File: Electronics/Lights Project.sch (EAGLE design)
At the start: 16 parts

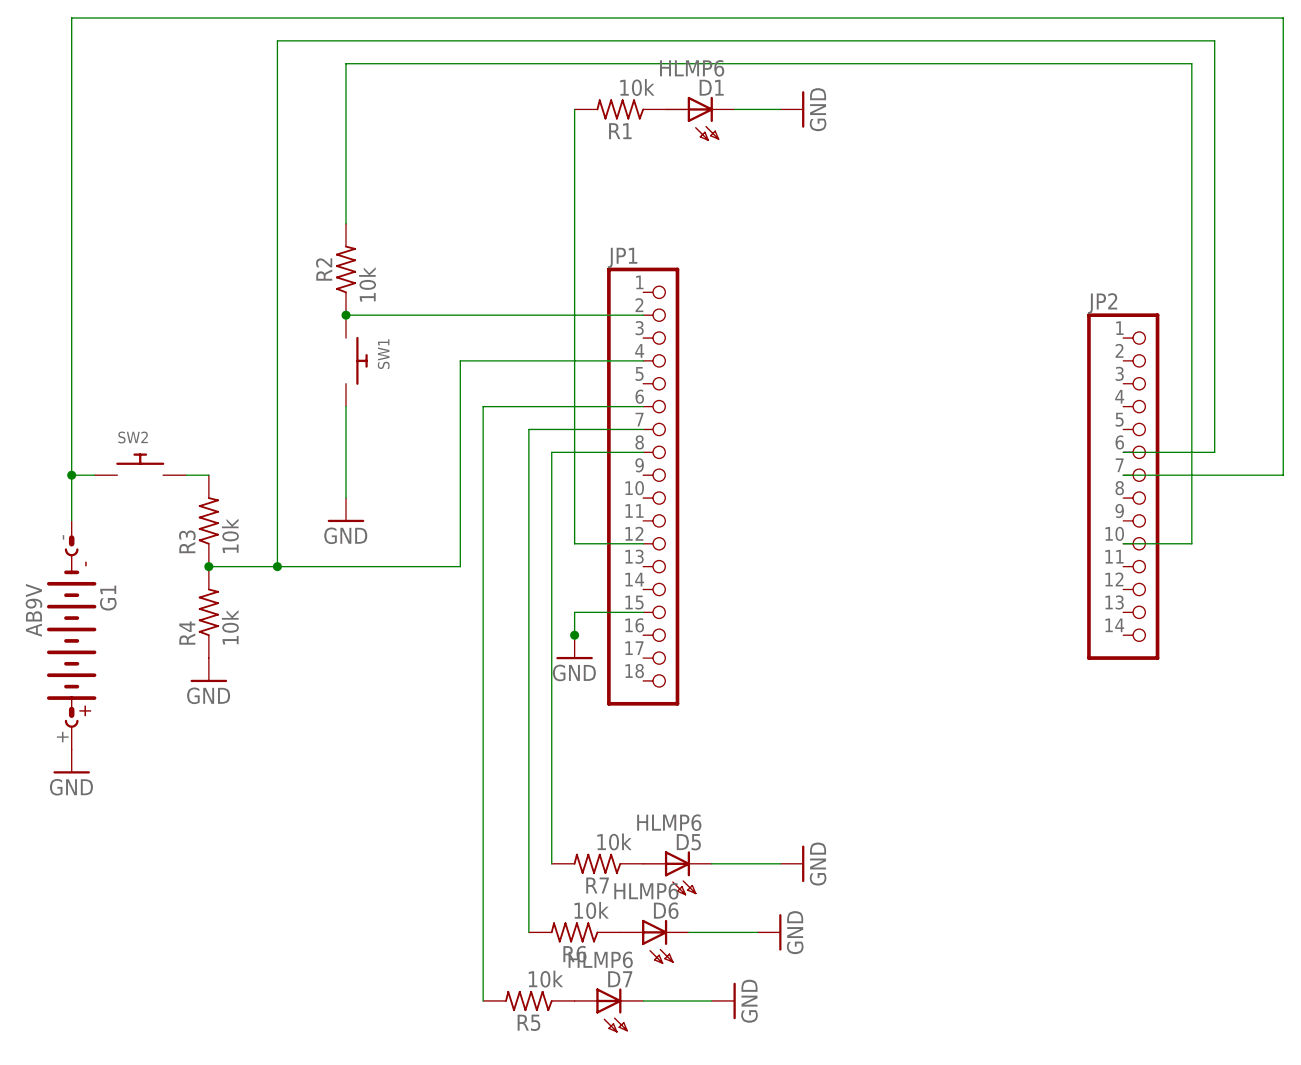
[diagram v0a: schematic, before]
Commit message: Updated PCB and Schematic: added headers and holes
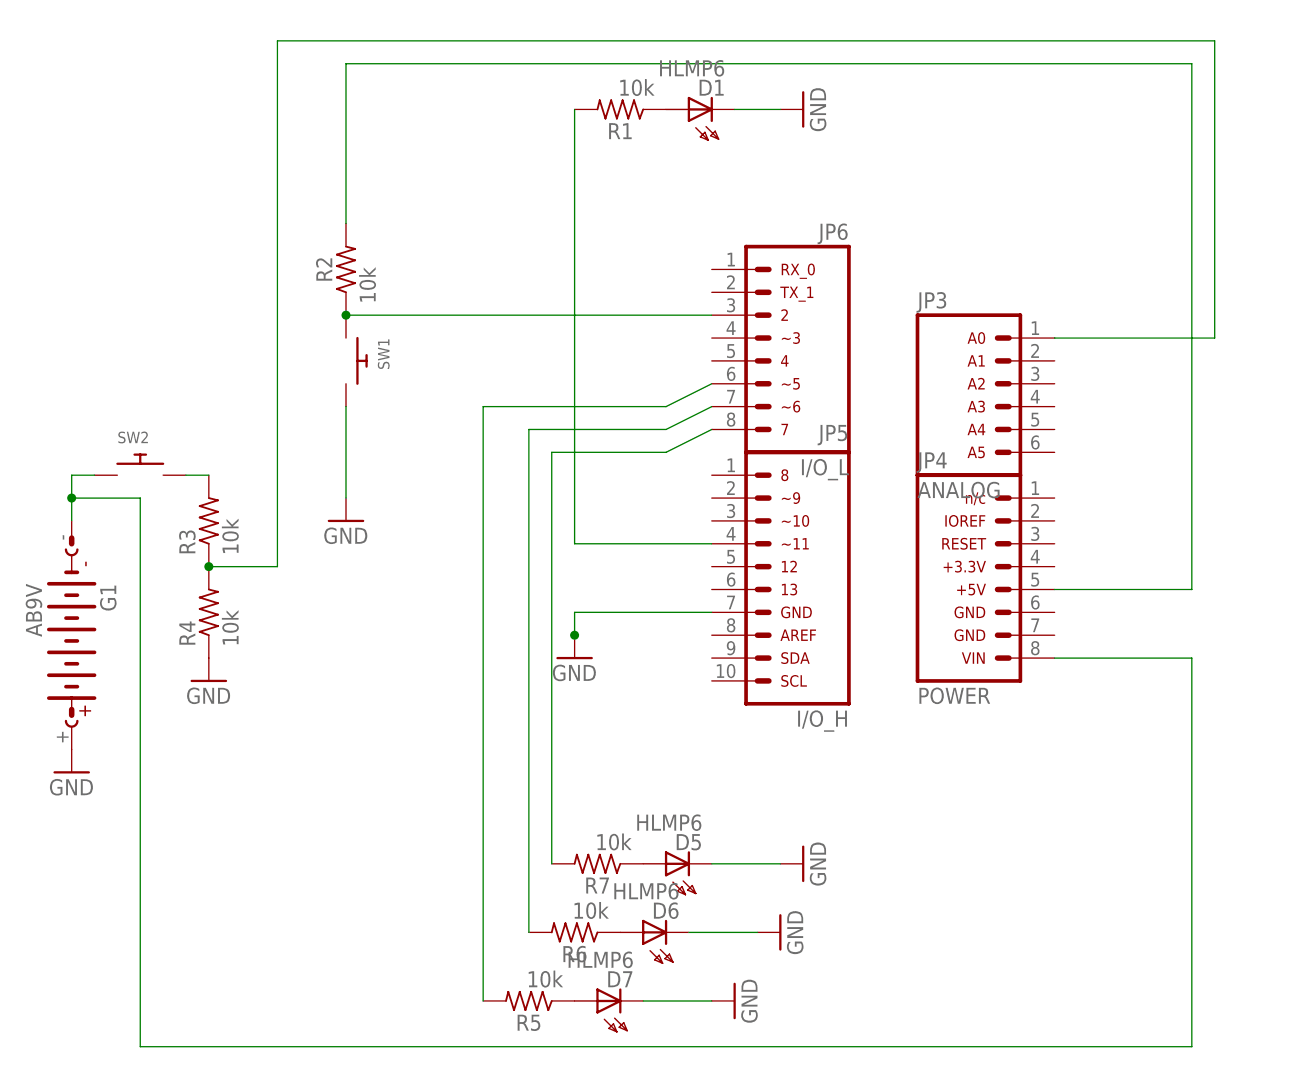
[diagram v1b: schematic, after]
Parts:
- removed JP1: (no value), adafruit:PINHD-1X18
- removed JP2: (no value), adafruit:PINHD-1X14
- added JP3: (no value), arduino_jw:ARDUINO_CONN-ANALOGSIP
- added JP4: (no value), arduino_jw:ARDUINO_CONN-POWERSIP
- added JP5: ARDUINO_CONN-IO_HSIP, arduino_jw:ARDUINO_CONN-IO_HSIP
- added JP6: (no value), arduino_jw:ARDUINO_CONN-IO_LSIP
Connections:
- net GND: now also JP5.7; no longer JP1.15
- net N$1: now also JP4.8; no longer JP2.7
- net N$10: now also JP6.7; no longer JP1.7
- net N$11: now also JP6.8; no longer JP1.8
- net N$13: now also JP3.1; no longer JP1.4, JP2.6
- net N$14: now also JP4.5; no longer JP2.10
- net N$2: now also JP5.4; no longer JP1.12
- net N$5: now also JP6.3; no longer JP1.2
- net N$8: now also JP6.6; no longer JP1.6
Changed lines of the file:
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@@
 <part name="GND10" library="supply1" library_urn="urn:adsk.eagle:library:371" deviceset="GND" device=""/>
 <part name="R7" library="rcl" library_urn="urn:adsk.eagle:library:334" deviceset="R-US_" device="R0805" package3d_urn="urn:adsk.eagle:package:23553/2" value="10k"/>
-<part name="JP1" library="adafruit" library_urn="urn:adsk.eagle:library:420" deviceset="PINHD-1X18" device="" package3d_urn="urn:adsk.eagle:package:6240826/1"/>
-<part name="JP2" library="adafruit" library_urn="urn:adsk.eagle:library:420" deviceset="PINHD-1X14" device="" package3d_urn="urn:adsk.eagle:package:6240769/1"/>
 <part name="D1" library="display-hp" library_urn="urn:adsk.eagle:library:212" deviceset="HLMP6" device="" package3d_urn="urn:adsk.eagle:package:12992/1"/>
 <part name="D5" library="display-hp" library_urn="urn:adsk.eagle:library:212" deviceset="HLMP6" device="" package3d_urn="urn:adsk.eagle:package:12992/1"/>
 <part name="D6" library="display-hp" library_urn="urn:adsk.eagle:library:212" deviceset="HLMP6" device="" package3d_urn="urn:adsk.eagle:package:12992/1"/>
 <part name="D7" library="display-hp" library_urn="urn:adsk.eagle:library:212" deviceset="HLMP6" device="" package3d_urn="urn:adsk.eagle:package:12992/1"/>
+<part name="JP3" library="arduino_jw" deviceset="ARDUINO_CONN-ANALOG" device="SIP"/>
+<part name="JP5" library="arduino_jw" deviceset="ARDUINO_CONN-IO_H" device="SIP"/>
+<part name="JP6" library="arduino_jw" deviceset="ARDUINO_CONN-IO_L" device="SIP"/>
+<part name="JP4" library="arduino_jw" deviceset="ARDUINO_CONN-POWER" device="SIP"/>
 </parts>
 <sheets>
@@
 <attribute name="NAME" x="63.5" y="-6.604" size="1.778" layer="95" font="vector" rot="R180" align="bottom-center"/>
 </instance>
-<instance part="JP1" gate="A" x="71.12" y="38.1">
-<attribute name="NAME" x="64.77" y="61.595" size="1.778" layer="95"/>
-<attribute name="VALUE" x="64.77" y="10.16" size="1.778" layer="96"/>
-</instance>
-<instance part="JP2" gate="A" x="124.46" y="38.1">
-<attribute name="NAME" x="118.11" y="56.515" size="1.778" layer="95"/>
-<attribute name="VALUE" x="118.11" y="15.24" size="1.778" layer="96"/>
-</instance>
 <instance part="D1" gate="A" x="76.2" y="78.74" rot="R90">
 <attribute name="NAME" x="77.724" y="82.042" size="1.778" layer="95" rot="R180"/>
@@
 <attribute name="NAME" x="67.564" y="-17.018" size="1.778" layer="95" rot="R180"/>
 <attribute name="VALUE" x="67.564" y="-14.859" size="1.778" layer="96" rot="R180"/>
+</instance>
+<instance part="JP3" gate="G$1" x="99.06" y="38.1">
+<attribute name="NAME" x="99.06" y="56.642" size="1.778" layer="95"/>
+</instance>
+<instance part="JP5" gate="G$1" x="91.44" y="12.7" rot="MR0">
+<attribute name="NAME" x="91.44" y="41.91" size="1.778" layer="95" rot="MR0"/>
+</instance>
+<instance part="JP6" gate="G$1" x="91.44" y="40.64" rot="MR0">
+<attribute name="NAME" x="91.44" y="64.262" size="1.778" layer="95" rot="MR0"/>
+</instance>
+<instance part="JP4" gate="G$1" x="99.06" y="15.24">
+<attribute name="NAME" x="99.06" y="38.862" size="1.778" layer="95"/>
 </instance>
 </instances>
@@
 <segment>
 <pinref part="G1" gate="G$1" pin="-"/>
-<wire x1="5.08" y1="33.02" x2="5.08" y2="38.1" width="0.1524" layer="91"/>
+<wire x1="5.08" y1="33.02" x2="5.08" y2="35.56" width="0.1524" layer="91"/>
 <pinref part="SW2" gate="G$1" pin="P$1"/>
+<wire x1="5.08" y1="35.56" x2="5.08" y2="38.1" width="0.1524" layer="91"/>
 <wire x1="5.08" y1="38.1" x2="7.62" y2="38.1" width="0.1524" layer="91"/>
-<junction x="5.08" y="38.1"/>
-<wire x1="5.08" y1="38.1" x2="5.08" y2="88.9" width="0.1524" layer="91"/>
-<wire x1="5.08" y1="88.9" x2="139.7" y2="88.9" width="0.1524" layer="91"/>
-<wire x1="139.7" y1="88.9" x2="139.7" y2="38.1" width="0.1524" layer="91"/>
-<pinref part="JP2" gate="A" pin="7"/>
-<wire x1="121.92" y1="38.1" x2="139.7" y2="38.1" width="0.1524" layer="91"/>
+<wire x1="129.54" y1="-25.4" x2="12.7" y2="-25.4" width="0.1524" layer="91"/>
+<wire x1="12.7" y1="-25.4" x2="12.7" y2="35.56" width="0.1524" layer="91"/>
+<wire x1="12.7" y1="35.56" x2="5.08" y2="35.56" width="0.1524" layer="91"/>
+<junction x="5.08" y="35.56"/>
+<pinref part="JP4" gate="G$1" pin="8"/>
+<wire x1="114.3" y1="17.78" x2="129.54" y2="17.78" width="0.1524" layer="91"/>
+<wire x1="129.54" y1="17.78" x2="129.54" y2="-25.4" width="0.1524" layer="91"/>
 </segment>
 </net>
@@
 <segment>
 <pinref part="SW1" gate="G$1" pin="P$1"/>
-<wire x1="35.56" y1="55.88" x2="68.58" y2="55.88" width="0.1524" layer="91"/>
+<wire x1="35.56" y1="55.88" x2="76.2" y2="55.88" width="0.1524" layer="91"/>
 <pinref part="R2" gate="G$1" pin="1"/>
 <junction x="35.56" y="55.88"/>
-<pinref part="JP1" gate="A" pin="2"/>
+<pinref part="JP6" gate="G$1" pin="3"/>
 </segment>
 </net>
@@
 <segment>
 <pinref part="GND4" gate="1" pin="GND"/>
-<pinref part="JP1" gate="A" pin="15"/>
 <wire x1="60.96" y1="20.32" x2="60.96" y2="22.86" width="0.1524" layer="91"/>
-<wire x1="60.96" y1="22.86" x2="68.58" y2="22.86" width="0.1524" layer="91"/>
 <junction x="60.96" y="20.32"/>
+<pinref part="JP5" gate="G$1" pin="7"/>
+<wire x1="76.2" y1="22.86" x2="60.96" y2="22.86" width="0.1524" layer="91"/>
 </segment>
 <segment>
@@
 <pinref part="R5" gate="G$1" pin="2"/>
 <wire x1="50.8" y1="-20.32" x2="50.8" y2="45.72" width="0.1524" layer="91"/>
-<wire x1="50.8" y1="45.72" x2="68.58" y2="45.72" width="0.1524" layer="91"/>
-<pinref part="JP1" gate="A" pin="6"/>
+<wire x1="50.8" y1="45.72" x2="71.12" y2="45.72" width="0.1524" layer="91"/>
+<pinref part="JP6" gate="G$1" pin="6"/>
+<wire x1="71.12" y1="45.72" x2="76.2" y2="48.26" width="0.1524" layer="91"/>
 </segment>
 </net>
@@
 <pinref part="R6" gate="G$1" pin="2"/>
 <wire x1="55.88" y1="-12.7" x2="55.88" y2="43.18" width="0.1524" layer="91"/>
-<wire x1="55.88" y1="43.18" x2="68.58" y2="43.18" width="0.1524" layer="91"/>
-<pinref part="JP1" gate="A" pin="7"/>
+<wire x1="55.88" y1="43.18" x2="71.12" y2="43.18" width="0.1524" layer="91"/>
+<pinref part="JP6" gate="G$1" pin="7"/>
+<wire x1="71.12" y1="43.18" x2="76.2" y2="45.72" width="0.1524" layer="91"/>
 </segment>
 </net>
 <net name="N$11" class="0">
 <segment>
-<wire x1="68.58" y1="40.64" x2="58.42" y2="40.64" width="0.1524" layer="91"/>
+<wire x1="71.12" y1="40.64" x2="58.42" y2="40.64" width="0.1524" layer="91"/>
 <wire x1="58.42" y1="40.64" x2="58.42" y2="-5.08" width="0.1524" layer="91"/>
 <pinref part="R7" gate="G$1" pin="2"/>
-<pinref part="JP1" gate="A" pin="8"/>
+<pinref part="JP6" gate="G$1" pin="8"/>
+<wire x1="71.12" y1="40.64" x2="76.2" y2="43.18" width="0.1524" layer="91"/>
 </segment>
 </net>
@@
 <wire x1="27.94" y1="27.94" x2="27.94" y2="86.36" width="0.1524" layer="91"/>
 <wire x1="27.94" y1="86.36" x2="132.08" y2="86.36" width="0.1524" layer="91"/>
-<wire x1="132.08" y1="86.36" x2="132.08" y2="40.64" width="0.1524" layer="91"/>
-<wire x1="27.94" y1="27.94" x2="48.26" y2="27.94" width="0.1524" layer="91"/>
-<junction x="27.94" y="27.94"/>
-<wire x1="48.26" y1="27.94" x2="48.26" y2="50.8" width="0.1524" layer="91"/>
-<wire x1="48.26" y1="50.8" x2="68.58" y2="50.8" width="0.1524" layer="91"/>
-<pinref part="JP1" gate="A" pin="4"/>
-<pinref part="JP2" gate="A" pin="6"/>
-<wire x1="121.92" y1="40.64" x2="132.08" y2="40.64" width="0.1524" layer="91"/>
+<wire x1="132.08" y1="86.36" x2="132.08" y2="53.34" width="0.1524" layer="91"/>
+<pinref part="JP3" gate="G$1" pin="1"/>
+<wire x1="114.3" y1="53.34" x2="132.08" y2="53.34" width="0.1524" layer="91"/>
 </segment>
 </net>
 <net name="N$2" class="0">
 <segment>
-<pinref part="JP1" gate="A" pin="12"/>
-<wire x1="68.58" y1="30.48" x2="60.96" y2="30.48" width="0.1524" layer="91"/>
 <pinref part="R1" gate="G$1" pin="2"/>
 <wire x1="60.96" y1="30.48" x2="60.96" y2="78.74" width="0.1524" layer="91"/>
+<pinref part="JP5" gate="G$1" pin="4"/>
+<wire x1="76.2" y1="30.48" x2="60.96" y2="30.48" width="0.1524" layer="91"/>
 </segment>
 </net>
@@
 <wire x1="35.56" y1="66.04" x2="35.56" y2="83.82" width="0.1524" layer="91"/>
 <wire x1="35.56" y1="83.82" x2="129.54" y2="83.82" width="0.1524" layer="91"/>
-<wire x1="129.54" y1="83.82" x2="129.54" y2="30.48" width="0.1524" layer="91"/>
-<pinref part="JP2" gate="A" pin="10"/>
-<wire x1="121.92" y1="30.48" x2="129.54" y2="30.48" width="0.1524" layer="91"/>
-</segment>
-</net>
+<pinref part="JP4" gate="G$1" pin="5"/>
+<wire x1="114.3" y1="25.4" x2="129.54" y2="25.4" width="0.1524" layer="91"/>
+<wire x1="129.54" y1="25.4" x2="129.54" y2="83.82" width="0.1524" layer="91"/>
+</segment>
+</net>
